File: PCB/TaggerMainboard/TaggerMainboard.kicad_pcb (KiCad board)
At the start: 2 copper layers, 63 parts, among them J3 DFPlayer, J5 USB_OTG, J6 ICSP, Q1 FDN304P, U1 MCU-ATMEGA2560-16AU(TQFP100), U2 IRLML2502, U3 LM2596S-5, U4 LMV358, U5 AMS1117-3.3, U6 FT232RL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

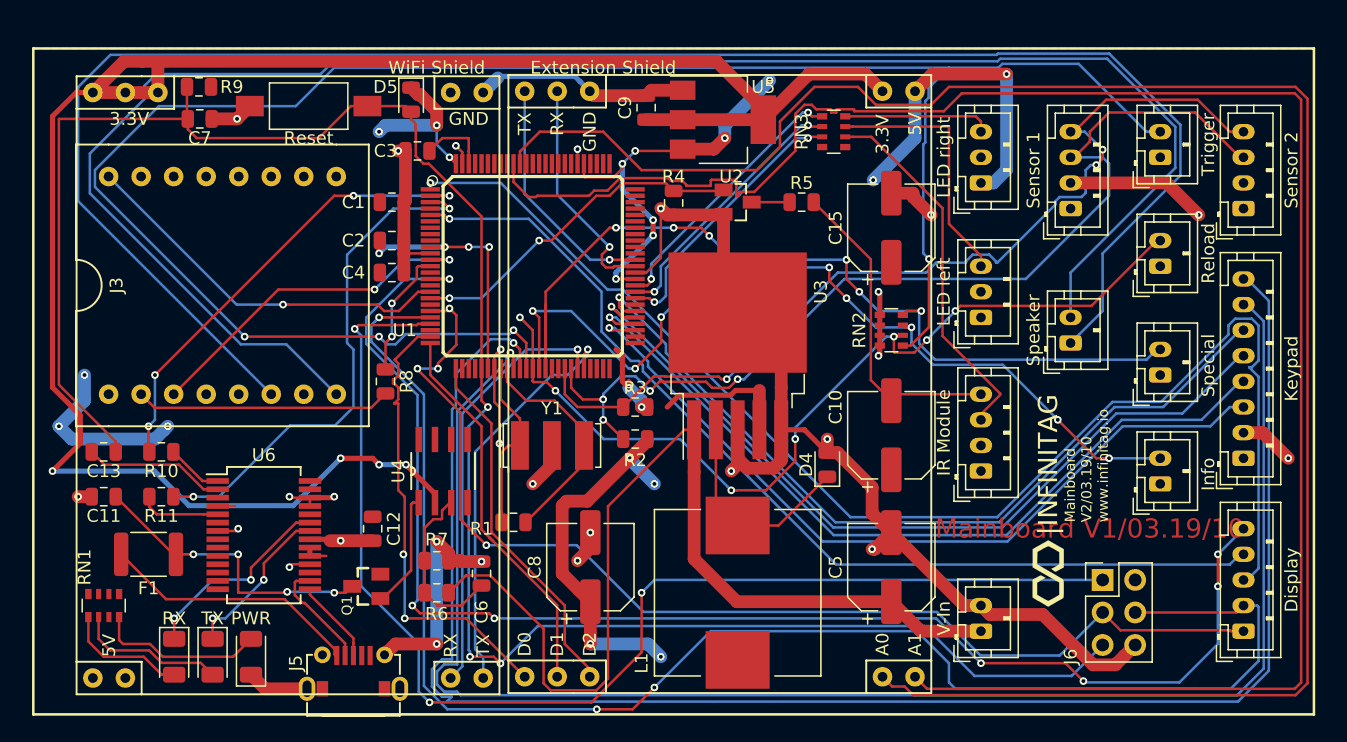
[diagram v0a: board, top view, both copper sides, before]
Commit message: Keypad + Bohrungen + Logo & Co
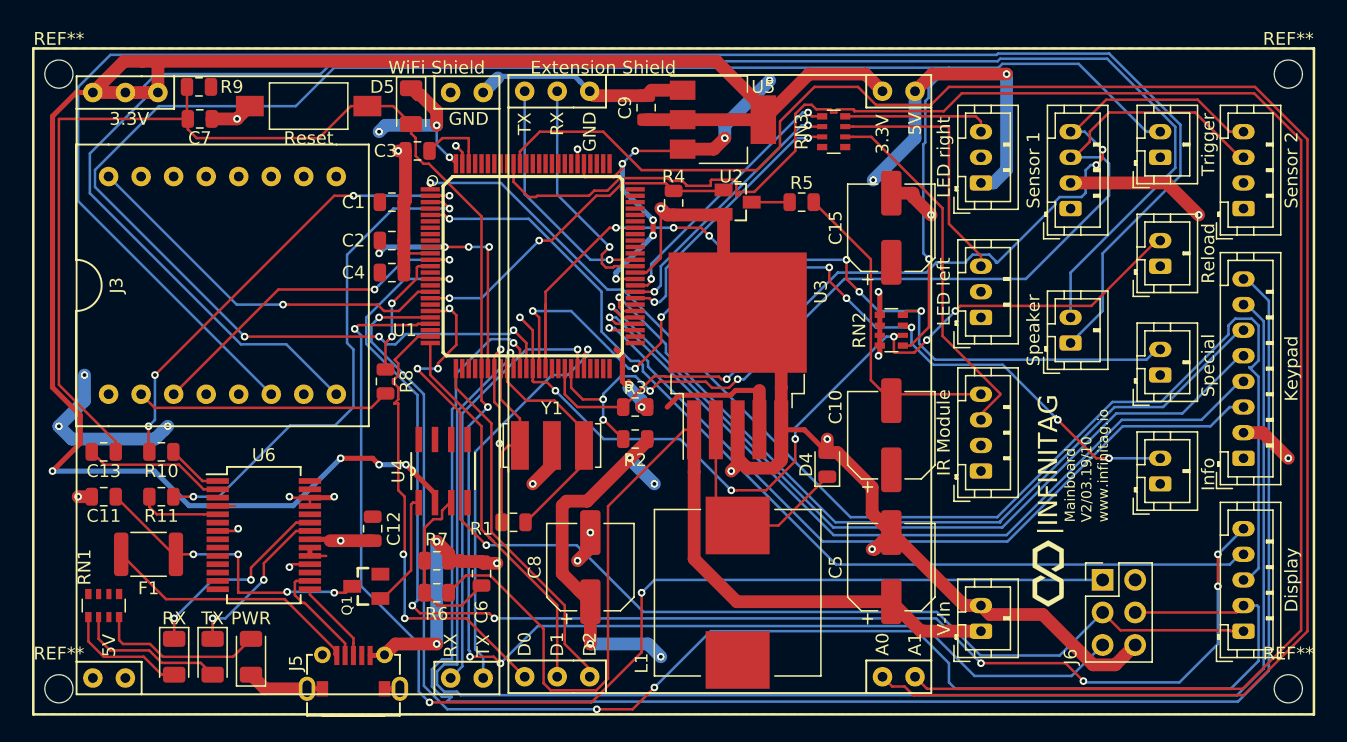
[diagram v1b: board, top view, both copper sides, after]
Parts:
- added REF**: MountingHole_2.2mm_M2_ISO7380, MountingHole:MountingHole_2.2mm_M2_ISO7380, F.Cu at (155.0, 45.0)
- added REF**: MountingHole_2.2mm_M2_ISO7380, MountingHole:MountingHole_2.2mm_M2_ISO7380, F.Cu at (155.0, 93.0)
- added REF**: MountingHole_2.2mm_M2_ISO7380, MountingHole:MountingHole_2.2mm_M2_ISO7380, F.Cu at (59.0, 45.0)
- added REF**: MountingHole_2.2mm_M2_ISO7380, MountingHole:MountingHole_2.2mm_M2_ISO7380, F.Cu at (59.0, 93.0)
- D5: footprint Diode_SMD:D_0805_2012Metric -> Diode_SMD:D_1206_3216Metric
- moved D5 0.50 mm to (86.5, 47.5)
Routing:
- net GND: track 196.6 -> 201.4 mm
- net Shield_A1: track 148.5 -> 144.2 mm
- net Shield_A0: track 149.6 -> 145.3 mm
- net RESET: track 159.6 -> 159.0 mm
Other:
- board text removed: "Mainboard V1/03.19/10"

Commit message: Anpassungen
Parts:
- D4: footprint Diode_SMD:D_0805_2012Metric -> Diode_SMD:D_SMA
- Y1: footprint Crystal:Resonator_SMD-3Pin_7.2x3.0mm -> Crystal:Resonator_SMD_muRata_CSTxExxV-3Pin_3.0x1.1mm
- moved D4 0.78 mm to (118.4, 75.0)
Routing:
- net GND: track 201.4 -> 206.0 mm
- net Net-(D4-Pad1): track 16.8 -> 19.5 mm
- net Net-(R1-Pad2): track 17.7 -> 16.6 mm
- net Net-(R1-Pad1): track 13.7 -> 14.5 mm
- net DF_TX: track 27.4 -> 27.9 mm
- net DF_SPK-: track 137.7 -> 138.2 mm
- net DF_SPK+: track 140.3 -> 140.8 mm
- net DF_BUSY: track 30.1 -> 30.6 mm
